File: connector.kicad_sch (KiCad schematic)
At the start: 4 parts, among them J1 Screw_Terminal_01x04

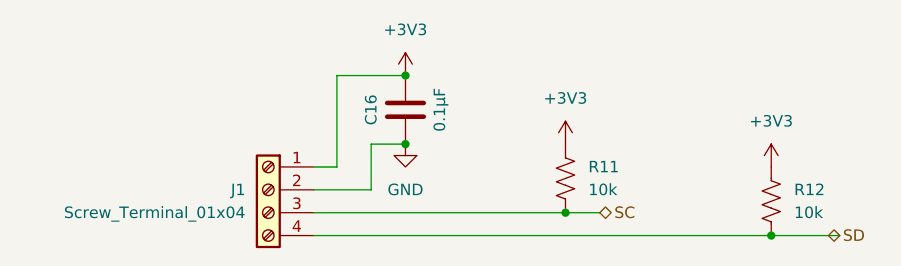
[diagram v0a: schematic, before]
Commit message: ERC and DRC warnings but not erros. Needs some layout adjustments.
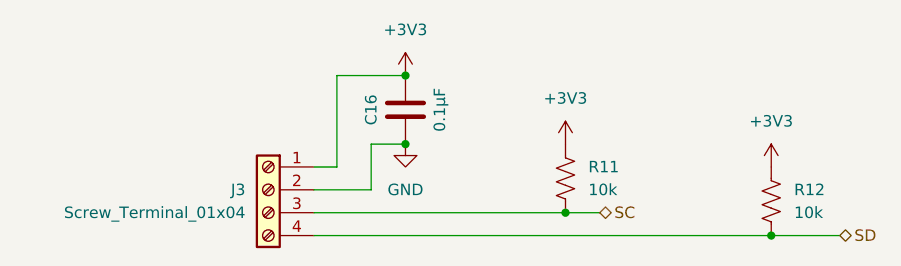
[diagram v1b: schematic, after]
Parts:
- renumbered J1 to J3
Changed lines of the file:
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@@
 	(hierarchical_label "SD"
 		(shape bidirectional)
-		(at 132.08 49.53 0)
+		(at 133.35 49.53 0)
 		(fields_autoplaced yes)
 		(effects
@@
 		(on_board yes)
 		(dnp no)
-		(property "Reference" "J1"
+		(property "Reference" "J3"
 			(at 67.31 44.4499 0)
 			(effects

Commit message: roughly complete, no errors or warnings.
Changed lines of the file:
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@@
 		(fields_autoplaced yes)
 		(property "Reference" "R11"
-			(at 105.41 41.91 0)
-			(effects
-				(font
-					(size 1.27 1.27)
-				)
-				(justify left)
+			(at 105.41 41.91 90)
+			(effects
+				(font
+					(size 1.27 1.27)
+				)
 			)
 		)
@@
 		(fields_autoplaced yes)
 		(property "Reference" "R12"
-			(at 128.27 44.45 0)
-			(effects
-				(font
-					(size 1.27 1.27)
-				)
-				(justify left)
+			(at 128.27 44.45 90)
+			(effects
+				(font
+					(size 1.27 1.27)
+				)
 			)
 		)
@@
 		(dnp no)
 		(property "Reference" "C16"
-			(at 81.28 35.56 90)
-			(effects
-				(font
-					(size 1.27 1.27)
-				)
+			(at 81.28 35.56 0)
+			(effects
+				(font
+					(size 1.27 1.27)
+				)
+				(justify left)
 			)
 		)
@@
 					(size 1.27 1.27)
 				)
-				(justify left)
-			)
-		)
+			)
+		)

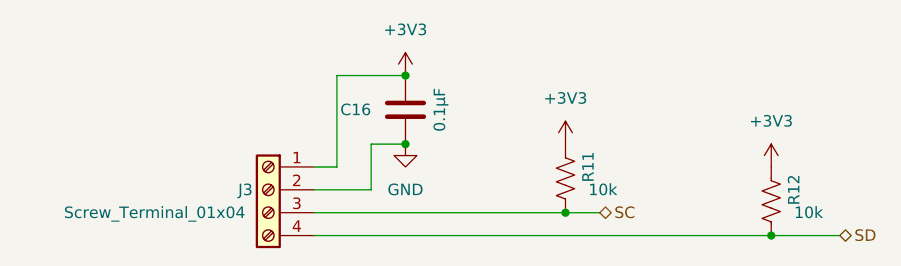
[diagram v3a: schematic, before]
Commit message: put masks on takeoffPads and other ongoing cleanup.
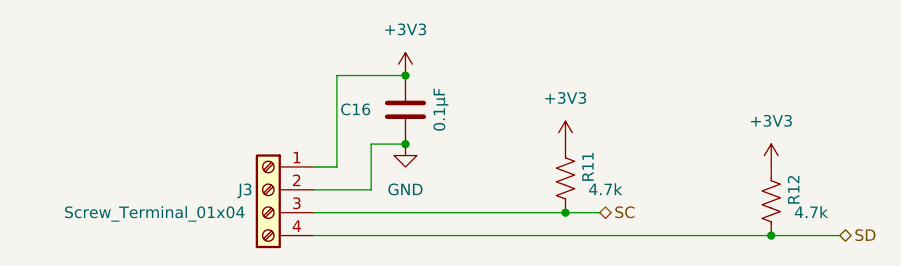
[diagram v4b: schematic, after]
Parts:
- R11, R12: value 10k -> 4.7k
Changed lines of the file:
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@@
 			)
 		)
-		(property "Value" "10k"
+		(property "Value" "4.7k"
 			(at 105.41 44.45 0)
 			(effects
@@
 			)
 		)
-		(property "Value" "10k"
+		(property "Value" "4.7k"
 			(at 128.27 46.99 0)
 			(effects

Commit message: clean up symbol fields
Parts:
- C16, R11, R12: MountType (none) -> SMT
- J3: Manufacturer (none) -> Cixi Kefa Elec; MfgPart (none) -> KF128-2.54-4P; MountType (none) -> PTH; Notes (none) -> or equivalent
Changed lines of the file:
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@@
+			)
+		)
+		(property "MountType" "SMT"
+			(at 102.87 43.18 0)
+			(effects
+				(font
+					(size 1.27 1.27)
+				)
+				(hide yes)
+			)
+		)
+		(property "Manufacturer" ""
+			(at 102.87 43.18 0)
+			(effects
+				(font
+					(size 1.27 1.27)
+				)
+				(hide yes)
+			)
+		)
+		(property "MfgPart" ""
+			(at 102.87 43.18 0)
+			(effects
+				(font
+					(size 1.27 1.27)
+				)
+				(hide yes)
+			)
+		)
+		(property "Notes" ""
+			(at 102.87 43.18 0)
+			(effects
+				(font
+					(size 1.27 1.27)
+				)
+				(hide yes)
 			)
 		)
@@
 			)
 		)
+		(property "MountType" "SMT"
+			(at 125.73 45.72 0)
+			(effects
+				(font
+					(size 1.27 1.27)
+				)
+				(hide yes)
+			)
+		)
+		(property "Manufacturer" ""
+			(at 125.73 45.72 0)
+			(effects
+				(font
+					(size 1.27 1.27)
+				)
+				(hide yes)
+			)
+		)
+		(property "MfgPart" ""
+			(at 125.73 45.72 0)
+			(effects
+				(font
+					(size 1.27 1.27)
+				)
+				(hide yes)
+			)
+		)
+		(property "Notes" ""
+			(at 125.73 45.72 0)
+			(effects
+				(font
+					(size 1.27 1.27)
+				)
+				(hide yes)
+			)
+		)
 		(pin "1"
 		)
@@
 			)
 		)
+		(property "MountType" "SMT"
+			(at 85.09 35.56 0)
+			(effects
+				(font
+					(size 1.27 1.27)
+				)
+				(hide yes)
+			)
+		)
+		(property "Manufacturer" ""
+			(at 85.09 35.56 0)
+			(effects
+				(font
+					(size 1.27 1.27)
+				)
+				(hide yes)
+			)
+		)
+		(property "MfgPart" ""
+			(at 85.09 35.56 0)
+			(effects
+				(font
+					(size 1.27 1.27)
+				)
+				(hide yes)
+			)
+		)
+		(property "Notes" ""
+			(at 85.09 35.56 0)
+			(effects
+				(font
+					(size 1.27 1.27)
+				)
+				(hide yes)
+			)
+		)
 		(pin "1"
 		)
@@
 			)
 		)
-		(property "Datasheet" "~"
+		(property "Datasheet" "https://www.lcsc.com/datasheet/lcsc_datasheet_2303171000_Cixi-Kefa-Elec-KF128-2-54-4P_C474922.pdf"
 			(at 69.85 44.45 0)
 			(effects
@@
 			(at 69.85 44.45 0)
 			(effects
+				(font
+					(size 1.27 1.27)
+				)
+				(hide yes)
+			)
+		)
+		(property "MountType" "PTH"
+			(at 69.85 44.45 0)
+			(effects
+				(font
+					(size 1.27 1.27)
+				)
+				(hide yes)
+			)
+		)
+		(property "Manufacturer" "Cixi Kefa Elec"
+			(at 69.85 44.45 0)
+			(effects
+				(font
+					(size 1.27 1.27)
+				)
+				(hide yes)
+			)
+		)
+		(property "MfgPart" "KF128-2.54-4P"
+			(at 69.85 44.45 0)
+			(effects
+				(font
+					(size 1.27 1.27)
+				)
+				(hide yes)
+			)
+		)
+		(property "Notes" "or equivalent"
+			(at 69.85 44.45 0)
+			(effects

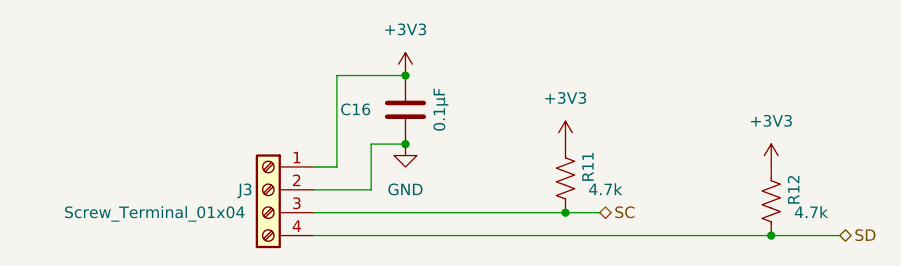
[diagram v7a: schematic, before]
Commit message: ongoing conversion to put f411 on board rather than pinsocket.
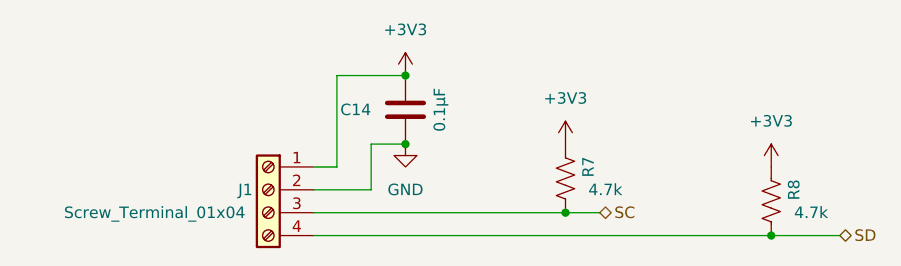
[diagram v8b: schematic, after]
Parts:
- renumbered C16 to C14, J3 to J1, R11 to R7, R12 to R8
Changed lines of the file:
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@@
 (kicad_sch
-	(version 20231120)
+	(version 20250114)
 	(generator "eeschema")
-	(generator_version "8.0")
+	(generator_version "9.0")
 	(paper "A4")
 	(title_block
@@
 		(shape bidirectional)
 		(at 106.68 46.99 0)
-		(fields_autoplaced yes)
 		(effects
 			(font
@@
 		(shape bidirectional)
 		(at 133.35 49.53 0)
-		(fields_autoplaced yes)
 		(effects
 			(font
@@
 		(dnp no)
 		(fields_autoplaced yes)
-		(property "Reference" "R11"
+		(property "Reference" "R7"
 			(at 105.41 41.91 90)
 			(effects
@@
 		(dnp no)
 		(fields_autoplaced yes)
-		(property "Reference" "#PWR051"
+		(property "Reference" "#PWR039"
 			(at 102.87 43.18 0)
 			(effects
@@
 		(on_board yes)
 		(dnp no)
-		(property "Reference" "#PWR047"
+		(property "Reference" "#PWR037"
 			(at 85.09 45.72 0)
 			(effects
@@
 		(dnp no)
 		(fields_autoplaced yes)
-		(property "Reference" "R12"
+		(property "Reference" "R8"
 			(at 128.27 44.45 90)
 			(effects
@@
 		(on_board yes)
 		(dnp no)
-		(property "Reference" "C16"
+		(property "Reference" "C14"
 			(at 81.28 35.56 0)
 			(effects
@@
 		(on_board yes)
 		(dnp no)
-		(property "Reference" "J3"
+		(property "Reference" "J1"
 			(at 67.31 44.4499 0)
 			(effects
@@
 		(dnp no)
 		(fields_autoplaced yes)
-		(property "Reference" "#PWR052"
+		(property "Reference" "#PWR044"
 			(at 125.73 45.72 0)
 			(effects
@@
 		(dnp no)
 		(fields_autoplaced yes)
-		(property "Reference" "#PWR048"
+		(property "Reference" "#PWR038"
 			(at 85.09 35.56 0)
 			(effects
